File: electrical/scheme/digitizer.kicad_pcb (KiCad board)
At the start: 2 copper layers, 229 parts, among them P1 mode, P10 in-2, P11 in-3, P12 in-1, P13 USB_B, P2 ~rst~, P3 ext, P4 trig, P5 trig-mode, P6 swd, P7 out-0, P8 out-1, P9 in-0, U1 AD8672, U10 crystal-4pin, U100 AD8672, U101 AD8672, U11 CP2102, U12 adr4533, U13 BAT54S, U14 adr4533, U15 ADT7410, U16 MCP1703T-3302E/CB, U17 AD7683, U18 NCP3063, U19 ADG5204, U2 AD8672, U20 NCP3063, U21 AD5543, U22 AD5543, U23 AD5543, U24 AD5543, U3 AD8672, U4 AD8672, U5 AD8672, U6 AD8672, U7 AD8672, U8 AD8672, U9 AD8672

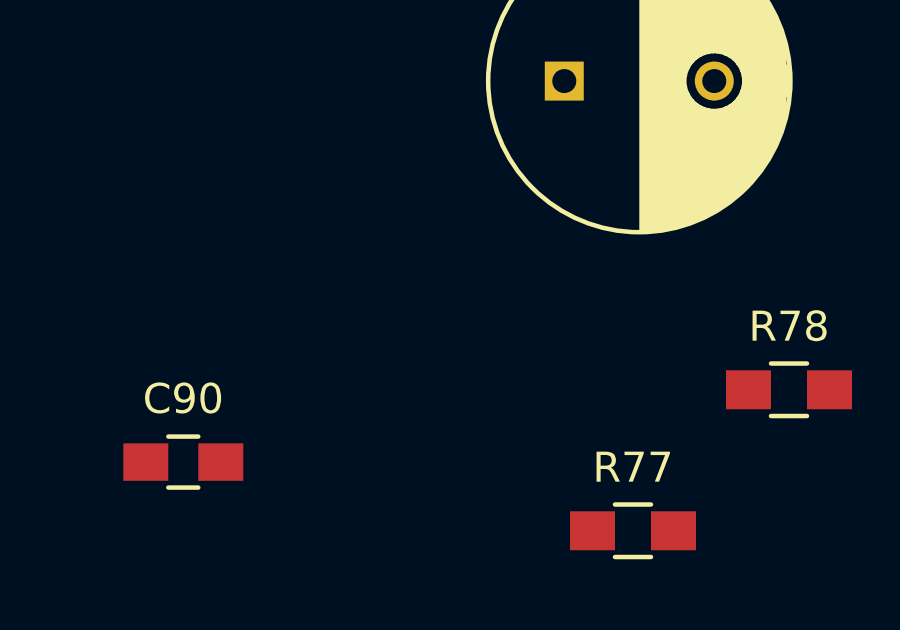
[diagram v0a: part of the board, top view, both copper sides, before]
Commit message: Added capacitors for making opamp driving capacitive load stable.
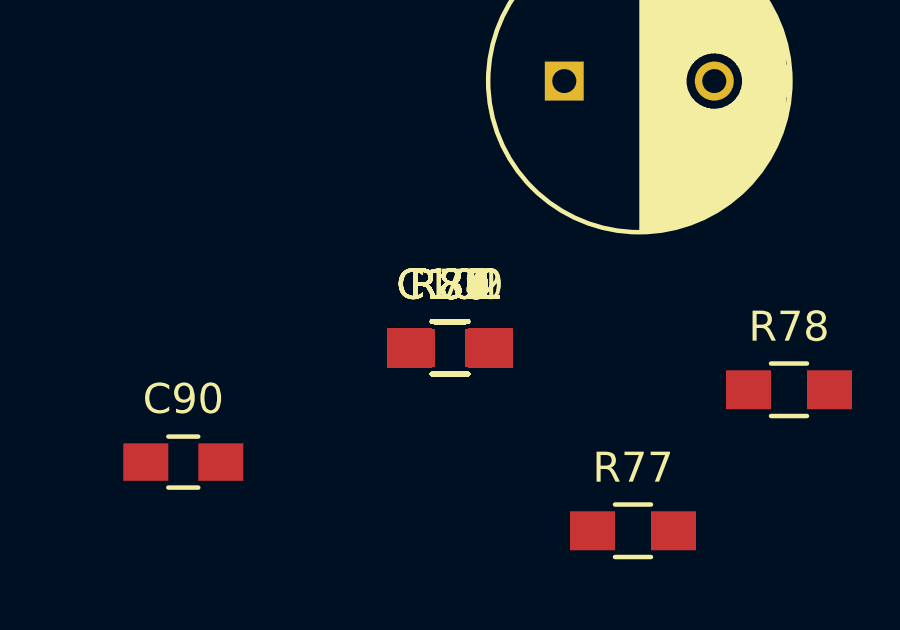
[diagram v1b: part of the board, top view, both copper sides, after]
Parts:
- added C100: 60p, Capacitors_SMD:C_0805_HandSoldering, F.Cu at (0.00, 0.00)
- added C101: 220p, Capacitors_SMD:C_0805_HandSoldering, F.Cu at (0.00, 0.00)
- added C102: 100p, Capacitors_SMD:C_0805_HandSoldering, F.Cu at (0.00, 0.00)
- added R79, R80, R81, R82, R83, R84, R85, R86, R87, R88, R89: 100 5%, Resistors_SMD:R_0805_HandSoldering, F.Cu at (0.00, 0.00)
- R15: value 50 5% -> 10 5%
- R77, R78: value 1k 5% -> 100 5%
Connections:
- R15 pad 1: Net-(R15-Pad1) -> Net-(C100-Pad2)
- R18 pad 2: Net-(R15-Pad1) -> Net-(C17-Pad1)
- R40 pad 2: Net-(R40-Pad2) -> Net-(P7-Pad1)
- R41 pad 2: Net-(R41-Pad2) -> Net-(P8-Pad1)
- R77 pad 1: Net-(R40-Pad2) -> Net-(C101-Pad2)
- R78 pad 1: Net-(R41-Pad2) -> Net-(C102-Pad2)
- U1 pad 7: Net-(R15-Pad1) -> Net-(C100-Pad2)
- U17 pad 5: /adc-cs -> Net-(R81-Pad2)
- U17 pad 6: /adc-miso -> Net-(R80-Pad2)
- U17 pad 7: /adc-sck -> Net-(R79-Pad2)
- U2 pad 7: Net-(R40-Pad2) -> Net-(C101-Pad2)
- U23 pad 1: /dac-v-0/sck -> /dac-v-1/sck
- U23 pad 2: /dac-v-0/mosi -> /dac-v-1/mosi
- U24 pad 1: /dac-v-0/sck -> /dac-v-1/sck
- U24 pad 2: /dac-v-0/mosi -> /dac-v-1/mosi
- U3 pad 7: Net-(R41-Pad2) -> Net-(C102-Pad2)
- stm321 pad 21: /dac-v-0/cs-2 -> /dac-cs-1
- stm321 pad 22: /dac-v-1/cs-1 -> /dac-cs-2
- stm321 pad 25: /dac-v-1/cs-2 -> /dac-cs-3
- stm321 pad 26: /dac-v-0/sck -> /dac-sck
- stm321 pad 28: /dac-v-0/mosi -> /dac-mosi
- stm321 pad 46: /dac-v-0/cs-1 -> /dac-cs-0

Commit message: a
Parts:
- added R90: 1k 5%, Resistors_SMD:R_0805_HandSoldering, F.Cu at (113.0, 150.0)
- added R91: 1k 5%, Resistors_SMD:R_0805_HandSoldering, F.Cu at (132.0, 150.0)
- added R92: 1k 5%, Resistors_SMD:R_0805_HandSoldering, F.Cu at (77.5, 141.5)
- added R93: 1k 5%, Resistors_SMD:R_0805_HandSoldering, F.Cu at (91.8, 143.2)
- moved P12 314.1 mm to (89.0, 161.5), turned to 180 degrees
- moved P11 279.4 mm to (127.5, 161.5), turned to 180 degrees
- moved P9 261.3 mm to (70.0, 161.5), turned to 180 degrees
- moved P7 254.3 mm to (151.0, 161.5), turned to 180 degrees
- moved P10 250.7 mm to (108.0, 161.5), turned to 180 degrees
- moved P8 250.4 mm to (170.0, 161.5), turned to 180 degrees
- moved C61 237.2 mm to (162.8, 122.8)
- moved C81 236.1 mm to (83.8, 145.0), turned to 180 degrees
- moved U100 234.3 mm to (84.5, 140.8)
- moved C83 234.0 mm to (85.8, 136.2)
- moved C62 220.6 mm to (156.8, 114.0), turned to 270 degrees
- moved C60 220.2 mm to (151.8, 119.2), turned to 180 degrees
- moved U4 219.3 mm to (73.0, 124.5)
- moved C53 213.1 mm to (141.8, 117.8)
- moved U101 212.4 mm to (138.8, 137.5)
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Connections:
- P10 pad 1: /in-2 -> Net-(P10-Pad1)
- P11 pad 1: /in-3 -> Net-(P11-Pad1)
- P12 pad 1: /in-1 -> Net-(P12-Pad1)
- P9 pad 1: /in-0 -> Net-(P9-Pad1)

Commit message: Inserted holding screw holes.
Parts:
- added P14: screw, Divers:douille_4mm, F.Cu at (172.5, 137.5)
- added P15: screw, Divers:douille_4mm, F.Cu at (67.5, 55.0)
- added P16: screw, Divers:douille_4mm, F.Cu at (172.5, 55.0)
- added P17: screw, Divers:douille_4mm, F.Cu at (67.5, 137.5)
- moved C40 163.0 mm to (67.5, 115.5)
- moved R46 27.0 mm to (76.5, 103.5), turned to 0 degrees
- moved C43 25.0 mm to (76.5, 106.0), turned to 0 degrees
- moved R47 24.0 mm to (66.0, 96.5), turned to 180 degrees
- moved C44 21.4 mm to (70.5, 97.0), turned to 270 degrees
- moved U4 20.6 mm to (71.0, 104.0), turned to 90 degrees
- moved R48 19.6 mm to (73.0, 97.0), turned to 90 degrees
- moved C42 18.8 mm to (65.5, 102.5), turned to 180 degrees
- moved R74 18.2 mm to (74.5, 148.0)
- moved R43 17.3 mm to (63.5, 117.0)
- moved R44 16.2 mm to (63.5, 112.0), turned to 270 degrees
- moved C45 16.2 mm to (76.5, 100.5), turned to 0 degrees
- moved R45 15.5 mm to (65.5, 105.0), turned to 0 degrees
- moved C41 14.8 mm to (67.5, 111.0), turned to 0 degrees
- moved C83 14.6 mm to (74.5, 145.5)
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
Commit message: a
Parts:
- moved C82 32.9 mm to (110.0, 144.5), turned to 0 degrees
- moved R72 31.9 mm to (110.0, 146.8), turned to 180 degrees
- moved U101 24.8 mm to (115.8, 146.8), turned to 90 degrees
- moved R71 18.7 mm to (121.2, 146.5), turned to 180 degrees
- moved R50 17.9 mm to (84.8, 130.8)
- moved C80 16.9 mm to (121.2, 148.8), turned to 180 degrees
- moved C49 16.6 mm to (92.2, 124.0)
- moved D1 16.4 mm to (63.2, 73.5), turned to 90 degrees
- moved R54 16.3 mm to (88.8, 115.0)
- moved R52 16.2 mm to (92.5, 121.5)
- moved R53 16.1 mm to (81.0, 126.0)
- moved U5 16.0 mm to (86.8, 122.0)
- moved C47 15.7 mm to (89.0, 129.2), turned to 0 degrees
- moved R49 15.7 mm to (84.8, 136.0)
- moved C48 15.4 mm to (81.2, 119.8)
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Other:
- board outline added: 120 x 120 mm

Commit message: a
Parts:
- moved R81 277.6 mm to (240.6, 115.6), turned to 180 degrees
- moved R80 270.9 mm to (240.6, 113.1), turned to 180 degrees
- moved C100 262.5 mm to (220.6, 113.6), turned to 90 degrees
- moved R79 260.8 mm to (240.6, 110.9), turned to 180 degrees
- moved C20 237.3 mm to (208.1, 113.6), turned to 270 degrees
- moved C16 230.8 mm to (232.4, 108.1), turned to 270 degrees
- moved C102 228.3 mm to (159.2, 143.5)
- moved C38 222.2 mm to (-119.2, 64.2)
- moved C71 218.5 mm to (142.0, 113.0)
- moved C30 215.2 mm to (133.8, 141.5), turned to 270 degrees
- moved C70 214.8 mm to (152.5, 117.0), turned to 180 degrees
- moved C19 214.3 mm to (210.4, 113.6), turned to 270 degrees
- moved C24 212.7 mm to (163.8, 139.8), turned to 180 degrees
- moved U2 212.0 mm to (142.5, 136.5), turned to 270 degrees
- moved C32 209.9 mm to (137.5, 139.8)
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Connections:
- U19 pad 10: /input-filter-attenuator-3/out -> /input-filter-attenuator-2/out
- U19 pad 11: /input-filter-attenuator-2/out -> /input-filter-attenuator-3/out
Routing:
- net /input-filter-attenuator-0/in: track 0.00 -> 35.9 mm
- net Net-(C50-Pad1): track 0.00 -> 28.2 mm
- net Net-(C44-Pad1): track 0.00 -> 27.6 mm
- net Net-(P12-Pad1): track 0.00 -> 14.4 mm
- net Net-(C46-Pad2): track 0.00 -> 13.1 mm
- net /in-0: track 0.00 -> 8.29 mm
- net Net-(C47-Pad1): track 0.00 -> 5.91 mm
- net Net-(C40-Pad2): track 0.00 -> 5.40 mm
- net Net-(P9-Pad1): track 0.00 -> 5.22 mm
- net /input-filter-attenuator-1/in: track 0.00 -> 4.93 mm
- net Net-(C51-Pad1): track 0.00 -> 4.58 mm
- net Net-(C46-Pad1): track 0.00 -> 4.44 mm
- net Net-(C45-Pad1): track 0.00 -> 4.43 mm
- net Net-(C43-Pad1): track 0.00 -> 4.41 mm
- net Net-(C41-Pad1): track 0.00 -> 4.40 mm
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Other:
- copper layers 2 -> 4

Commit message: a
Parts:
- moved C29 211.3 mm to (215.5, 81.0)
- moved C28 198.3 mm to (226.0, 85.5), turned to 180 degrees
- moved C35 132.5 mm to (219.0, 72.8)
- moved U19 132.5 mm to (226.0, 74.0)
- moved C34 132.2 mm to (233.0, 73.0)
- moved R18 99.7 mm to (223.2, 90.8)
- moved R31 90.1 mm to (226.0, 83.5)
- moved R32 86.0 mm to (215.5, 83.0)
- moved R25 34.3 mm to (226.0, 80.2), turned to 180 degrees
- moved C14 32.8 mm to (238.2, 84.2), turned to 90 degrees
- moved C19 28.1 mm to (215.5, 86.0), turned to 180 degrees
- moved C20 26.7 mm to (215.5, 88.0), turned to 180 degrees
- moved R33 25.6 mm to (219.0, 76.2)
- moved C17 25.4 mm to (228.0, 90.8), turned to 0 degrees
- moved C100 25.1 mm to (221.2, 88.5), turned to 0 degrees
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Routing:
- net Net-(C62-Pad1): track 0.00 -> 24.9 mm
- net Net-(C56-Pad1): track 0.00 -> 23.3 mm
- net Net-(P11-Pad1): track 0.00 -> 14.6 mm
- net /input-filter-attenuator-2/in: track 0.00 -> 13.9 mm
- net /in-2: track 0.00 -> 9.44 mm
- net Net-(C52-Pad2): track 0.00 -> 6.13 mm
- net Net-(C58-Pad2): track 0.00 -> 6.05 mm
- net Net-(C53-Pad1): track 0.00 -> 5.28 mm
- net Net-(P10-Pad1): track 0.00 -> 5.00 mm
- net Net-(C59-Pad1): track 0.00 -> 4.91 mm
- net Net-(C80-Pad2): track 0.00 -> 4.72 mm
- net Net-(C82-Pad2): track 0.00 -> 4.66 mm
- net Net-(C57-Pad1): track 0.00 -> 4.61 mm
- net Net-(C63-Pad1): track 0.00 -> 4.61 mm
- net Net-(C52-Pad1): track 0.00 -> 4.33 mm
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
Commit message: a
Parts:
- added R94: 100 5%, Resistors_SMD:R_0805_HandSoldering, F.Cu at (90.7, 100.5)
- added R95: 100 5%, Resistors_SMD:R_0805_HandSoldering, F.Cu at (99.0, 100.4)
- moved C14 135.1 mm to (106.7, 114.8)
- moved C15 135.1 mm to (102.2, 114.8)
- moved C16 135.1 mm to (104.2, 114.8)
- moved R79 135.1 mm to (111.2, 117.5)
- moved R80 135.1 mm to (111.2, 119.5)
- moved R81 135.1 mm to (111.2, 121.5)
- moved U17 135.1 mm to (104.3, 119.1)
- moved C34 134.5 mm to (102.3, 104.6)
- moved C35 134.5 mm to (88.3, 104.3)
- moved R33 134.5 mm to (88.3, 107.8)
- moved U19 134.5 mm to (95.3, 105.6)
- moved C100 133.8 mm to (91.0, 119.0)
- moved C19 133.8 mm to (85.2, 116.5)
- moved C20 133.8 mm to (85.2, 118.5)
- moved C28 133.8 mm to (95.8, 116.0)
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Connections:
- U19 pad 1: /adc-mux-0 -> Net-(R94-Pad1)
- U19 pad 14: /adc-mux-1 -> Net-(R95-Pad1)
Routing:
- net /input-filter-attenuator-1/out: track 3.58 -> 43.6 mm, vias 0 -> 2
- net /input-filter-attenuator-3/out: track 3.87 -> 39.0 mm, vias 0 -> 2
- net /input-filter-attenuator-2/out: track 3.87 -> 32.9 mm, vias 0 -> 2
- net /input-filter-attenuator-0/out: track 3.58 -> 31.7 mm, vias 0 -> 2
- net Net-(C100-Pad1): track 0.00 -> 16.9 mm
- net /dac-v-0/v-: track 0.00 -> 11.3 mm
- net Net-(C17-Pad1): track 0.00 -> 9.28 mm
- net Net-(C19-Pad1): track 0.00 -> 8.16 mm
- net Net-(R33-Pad1): track 0.00 -> 6.38 mm
- net Net-(C100-Pad2): track 0.00 -> 5.16 mm
- net Net-(C29-Pad2): track 0.00 -> 4.32 mm
- net Net-(C28-Pad2): track 0.00 -> 4.32 mm
- net /adc-ref: track 0.00 -> 4.18 mm
- net Net-(C44-Pad1): track 27.6 -> 31.7 mm
- net GNDA: track 2.00 -> 6.04 mm
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
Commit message: a
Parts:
- moved L5 394.7 mm to (275.0, 98.2), turned to 90 degrees
- moved C88 387.1 mm to (273.2, 92.4), turned to 180 degrees
- moved C39 385.5 mm to (268.0, 95.7), turned to 270 degrees
- moved C89 373.1 mm to (265.7, 85.9), turned to 0 degrees
- moved C90 373.0 mm to (273.2, 77.6), turned to 180 degrees
- moved C36 370.9 mm to (259.7, 86.8)
- moved C37 370.9 mm to (249.4, 86.5)
- moved C38 370.9 mm to (250.3, 94.7)
- moved D4 370.9 mm to (246.6, 80.3)
- moved L2 370.9 mm to (252.7, 75.3)
- moved R38 370.9 mm to (259.7, 81.8)
- moved R39 370.9 mm to (256.0, 90.5)
- moved R42 370.9 mm to (252.3, 90.5)
- moved U20 370.9 mm to (254.4, 84.2)
- moved C91 358.7 mm to (265.7, 71.9), turned to 0 degrees
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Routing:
- net Net-(P8-Pad1): track 0.00 -> 16.5 mm
- net Net-(P7-Pad1): track 0.00 -> 15.4 mm
- net Net-(C102-Pad1): track 0.00 -> 13.7 mm
- net Net-(C101-Pad1): track 0.00 -> 13.5 mm
- net Net-(R36-Pad1): track 0.00 -> 13.1 mm
- net Net-(R34-Pad1): track 0.00 -> 12.5 mm
- net GNDA: track 6.04 -> 14.0 mm
- net Net-(R23-Pad1): track 0.00 -> 5.83 mm
- net Net-(R21-Pad1): track 0.00 -> 5.62 mm
- net Net-(C101-Pad2): track 0.00 -> 4.50 mm
- net Net-(C24-Pad2): track 0.00 -> 4.36 mm
- net Net-(C58-Pad1): track 0.00 -> 4.35 mm
- net Net-(C102-Pad2): track 0.00 -> 4.23 mm
- net /dac-v-0/dac-ref: track 0.00 -> 4.23 mm
- net Net-(C26-Pad2): track 0.00 -> 4.09 mm
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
